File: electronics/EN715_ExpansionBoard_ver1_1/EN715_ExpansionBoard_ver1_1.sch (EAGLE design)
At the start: 46 parts, among them IC1 FE1.1S, M1 MPU9250_MODULE

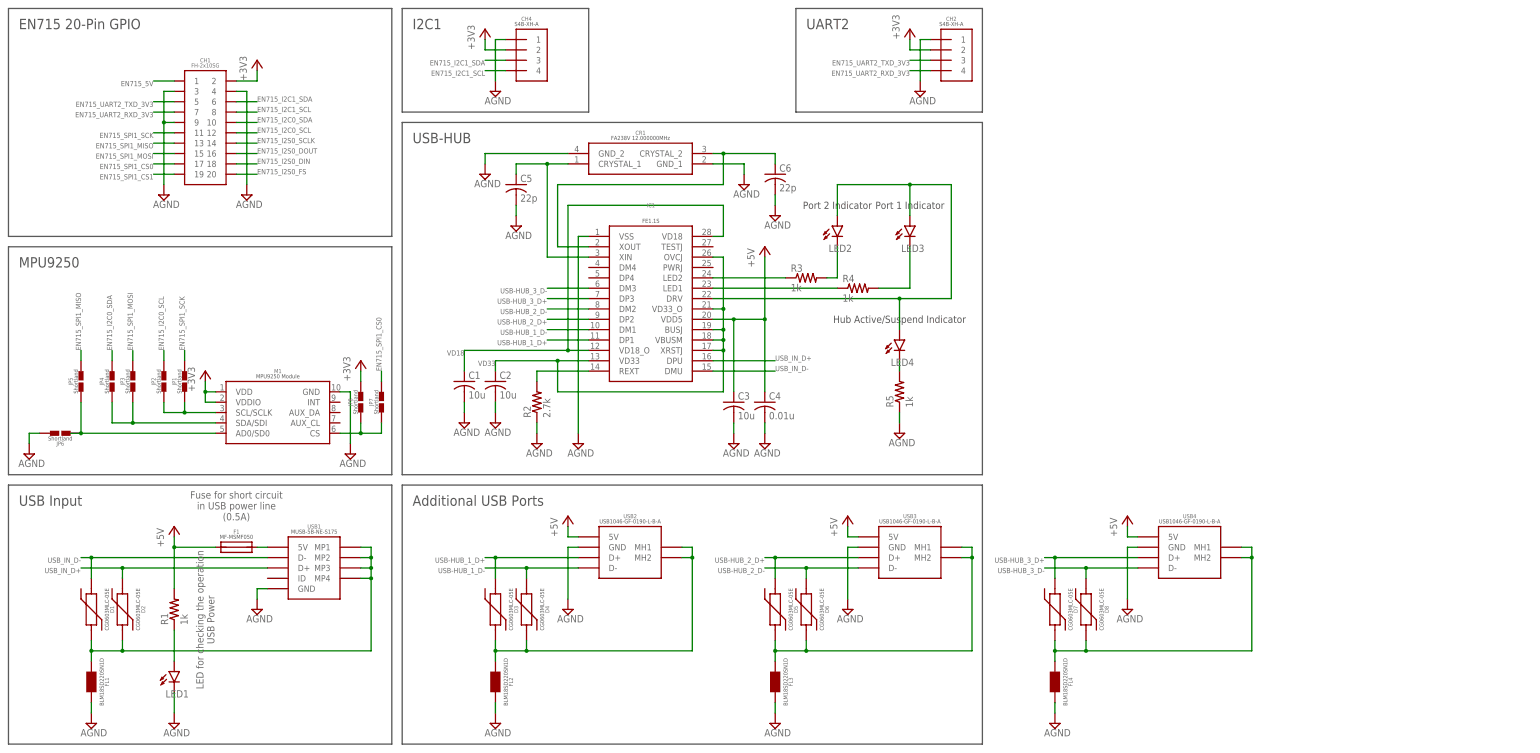
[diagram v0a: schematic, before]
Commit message: Created an Expansion Board with 4 USB-HUBs
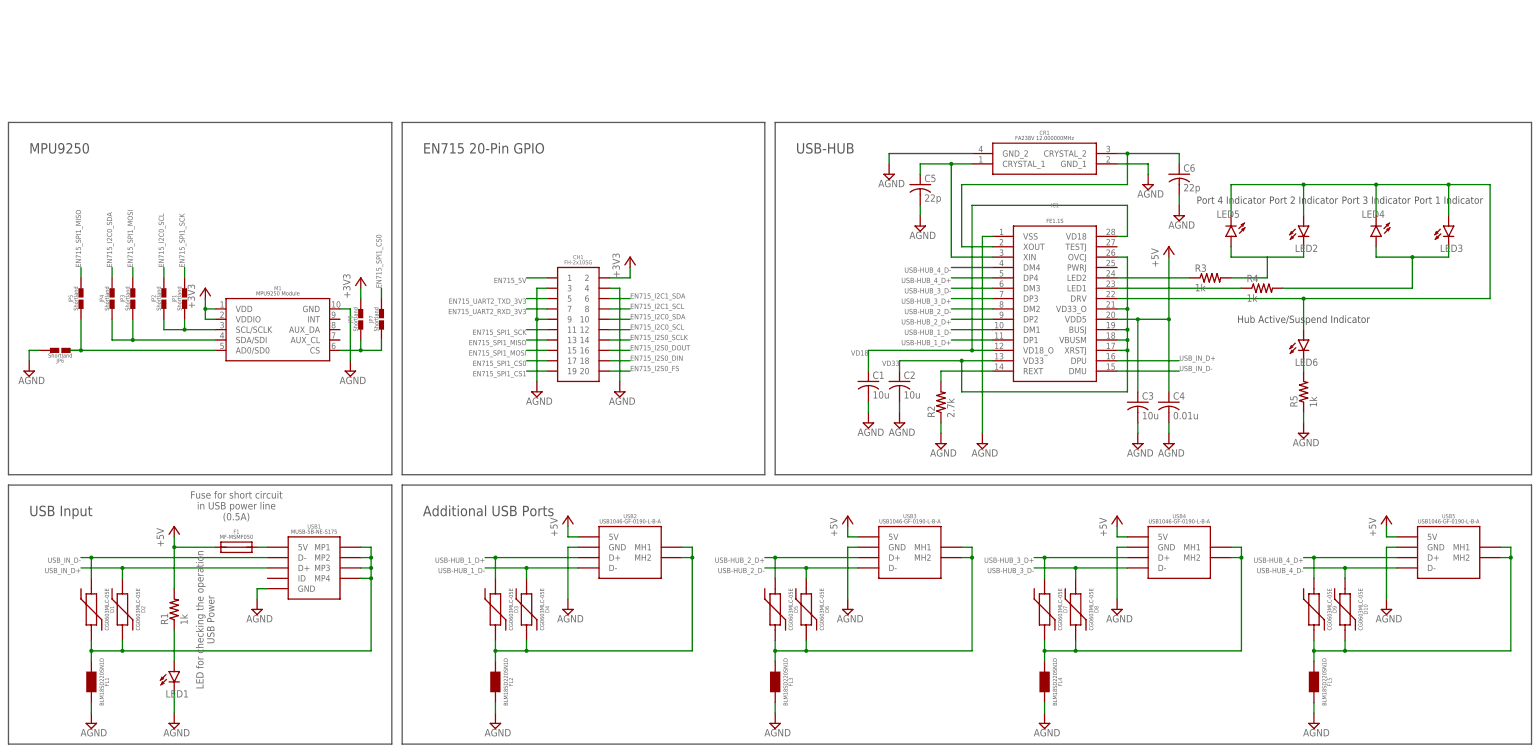
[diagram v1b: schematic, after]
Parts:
- removed CH2, CH4: S4B-XH-A, JST-XH:S4B-XH-A
- added D10, D9: CG0603MLC-05E, CG0603MLC-05E:CG0603MLC-05E
- added FL5: BLM18SD220SN1D, BLM18SD220SN1D:BLM18SD220SN1D
- added LED5, LED6: (no value), led:LEDSML0603
- added USB5: USB_A_X1_SMD, USB_Connector:USB_A_X1_SMD
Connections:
- net USB_A_2_SHIELD1 renamed USB_A_3_SHIELD
- new net USB-HUB_4_D+: D9.1, IC1.DP4, USB5.D+
- new net USB-HUB_4_D-: D10.1, IC1.DM4, USB5.D-
- new net USB_A_4_SHIELD: D10.2, D9.2, FL5.1, USB5.MH1, USB5.MH2
- net +3V3: no longer CH2.2, CH4.2
- net +5V: now also USB5.5V
- net AGND: now also FL5.2, USB5.GND; no longer CH2.1, CH4.1
- net EN715_I2C1_SCL: no longer CH4.4
- net EN715_I2C1_SDA: no longer CH4.3
- net EN715_UART2_RXD_3V3: no longer CH2.4
- net EN715_UART2_TXD_3V3: no longer CH2.3
- net FE1.1S_DRV: now also LED4.C, LED5.C, LED6.A; no longer LED4.A
- net FE1.1S_DRV_LED_A: now also LED6.C; no longer LED4.C
- net FE1.1S_LED1_A: now also LED4.A
- net FE1.1S_LED_2_A: now also LED5.A
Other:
- note added: "Port 3 Indicator"
- note added: "Port 4 Indicator"
- note removed: "I2C1"
- note removed: "UART2"
- moved on the sheet: C1, C2, C3, C4, C5, C6, CH1, CR1, D7, D8, FL4, IC1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

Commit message: Organizing Files
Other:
- note added: "1.1"
- note added: "1/1"
- note added: "April 26, 2022"
- note added: "EN715 ExpansionBoard"
- note added: "External AverMedia CarrierBoard EN715 GPIO Pins"
- note added: "External StrawberryLinux MPU-9250 9DOF sensor module"
- note added: "USB2.0 4 Ports HUB"
- note added: "USB2.0 HUB Input"
- note removed: "EN715 20-Pin GPIO"
- note removed: "MPU9250"
- note removed: "USB Input"
- note removed: "USB-HUB"
- moved on the sheet: C1, C2, C3, C4, C5, C6, CH1, CR1, D1, D10, D2, D3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
